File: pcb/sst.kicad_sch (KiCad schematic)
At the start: 0 parts

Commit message: кристалл и I2C на схеме
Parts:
- added C1, C2: C, symbol Device_GOST:C
- added R? (x2): R, symbol Device_GOST:R
- added U1: ATmega328P-P, Package_DIP:DIP-28_W7.62mm, symbol sst:ATmega328P-P
- added X?: CONN_I2C, symbol sst:CONN_I2C
- added ZQ1: ZQ_CRYSTAL, symbol Device_GOST:ZQ_CRYSTAL
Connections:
- new net: R?.1, U1.2 (PD0), X?.1, X?.2
- new net: R?.1, U1.3 (PD1), X?.3, X?.4
- new net: C1.1, C2.2, U1.10 (XTAL2/PB7), U1.22 (GND), U1.8 (GND), U1.9 (XTAL1/PB6), ZQ1.1, ZQ1.2
- new net +5V: R?.2, R?.2, X?.6, X?.7
- new net GND: C1.2, C2.1, X?.5, X?.8

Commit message: placed buzzer
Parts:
- added HA?: Buzzer, symbol sst:Buzzer
- added HL?: HL_LED, symbol Device_GOST:HL_LED
- added R? (x2): R, symbol Device_GOST:R
- added SA?: SA_SPDT, symbol Device_GOST:SA_SPDT
- added VT?: 2N7000, Package_TO_SOT_THT:TO-92, symbol sst:2N7000
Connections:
- net +5V: now also R?.2, SA?.2
- net GND: now also R?.1, VT?.1 (S1)
- net SDA: now reaches R?.1, U1.2 (PD0), X?.1, X?.2
- net SCL: now reaches R?.1, U1.3 (PD1), X?.3, X?.4
- net at U1.4 (PD2): now also R?.2, VT?.2 (G1)
- new net: HA?.1 (+), SA?.1
- new net: HA?.2 (-), HL?.1 (K), VT?.6 (D1)
- new net: HL?.2 (A), R?.1

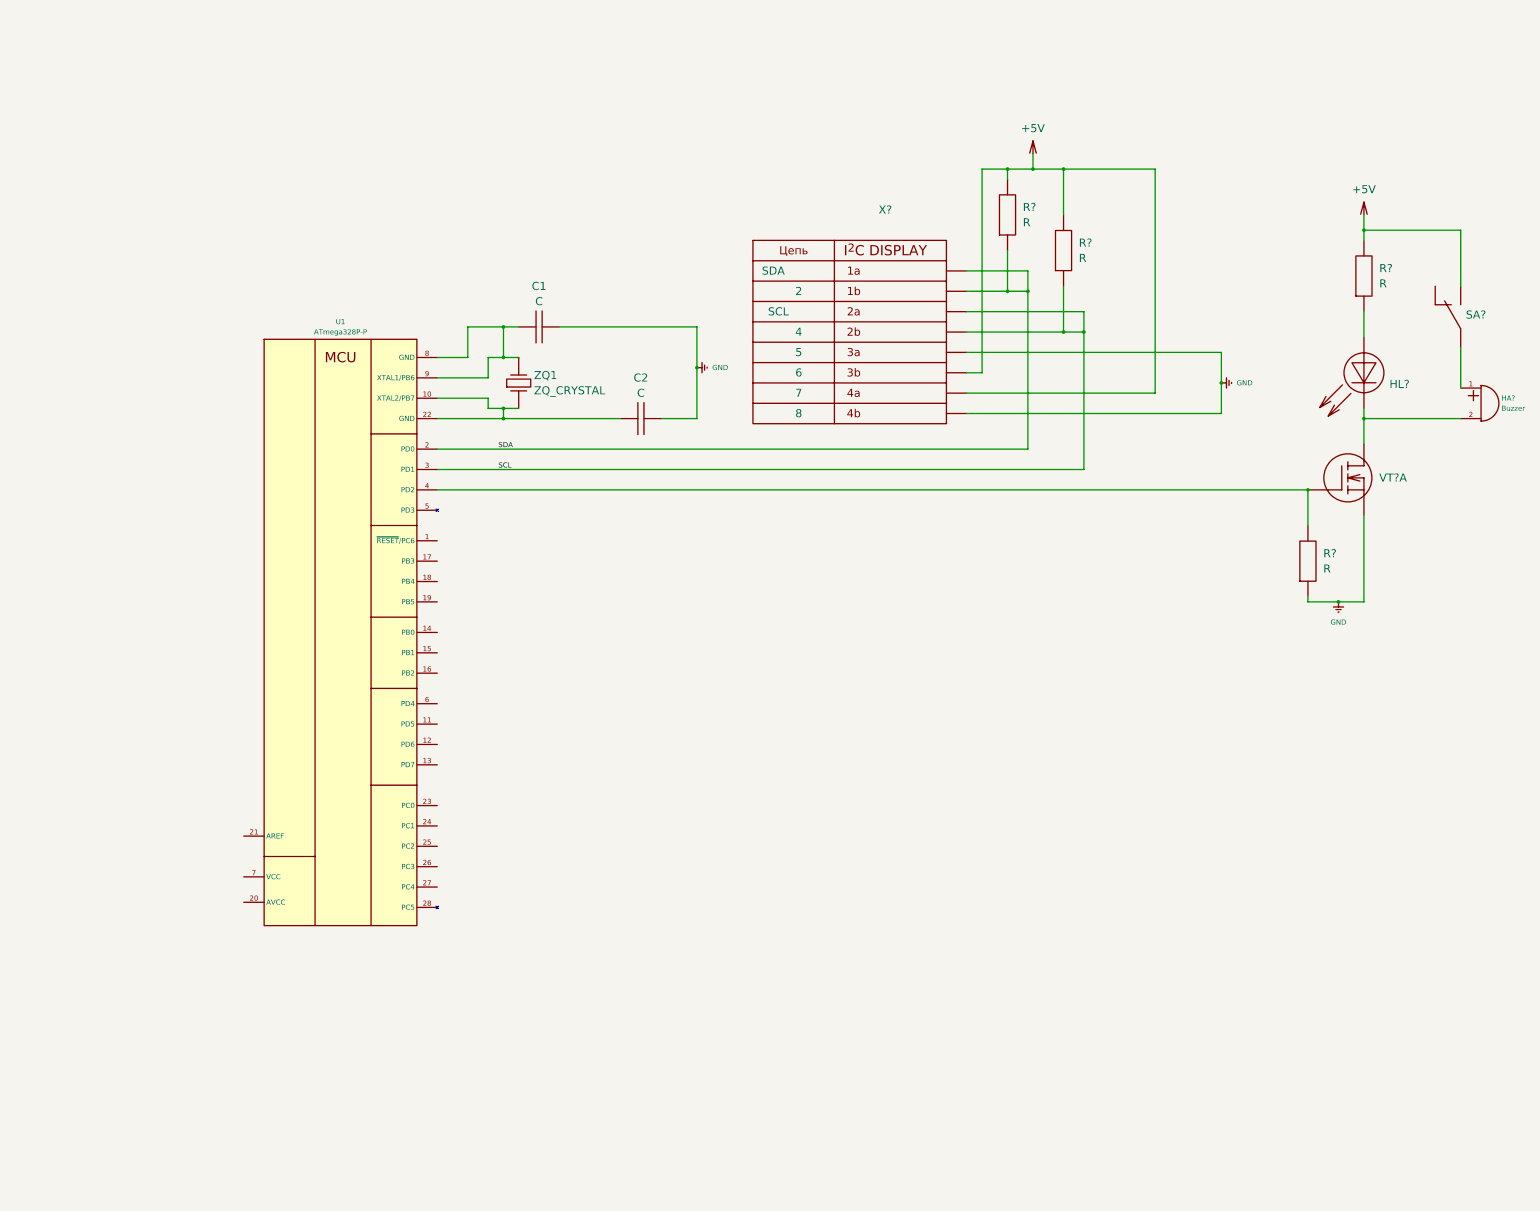
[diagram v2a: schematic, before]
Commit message: Входы на микроконтроллере
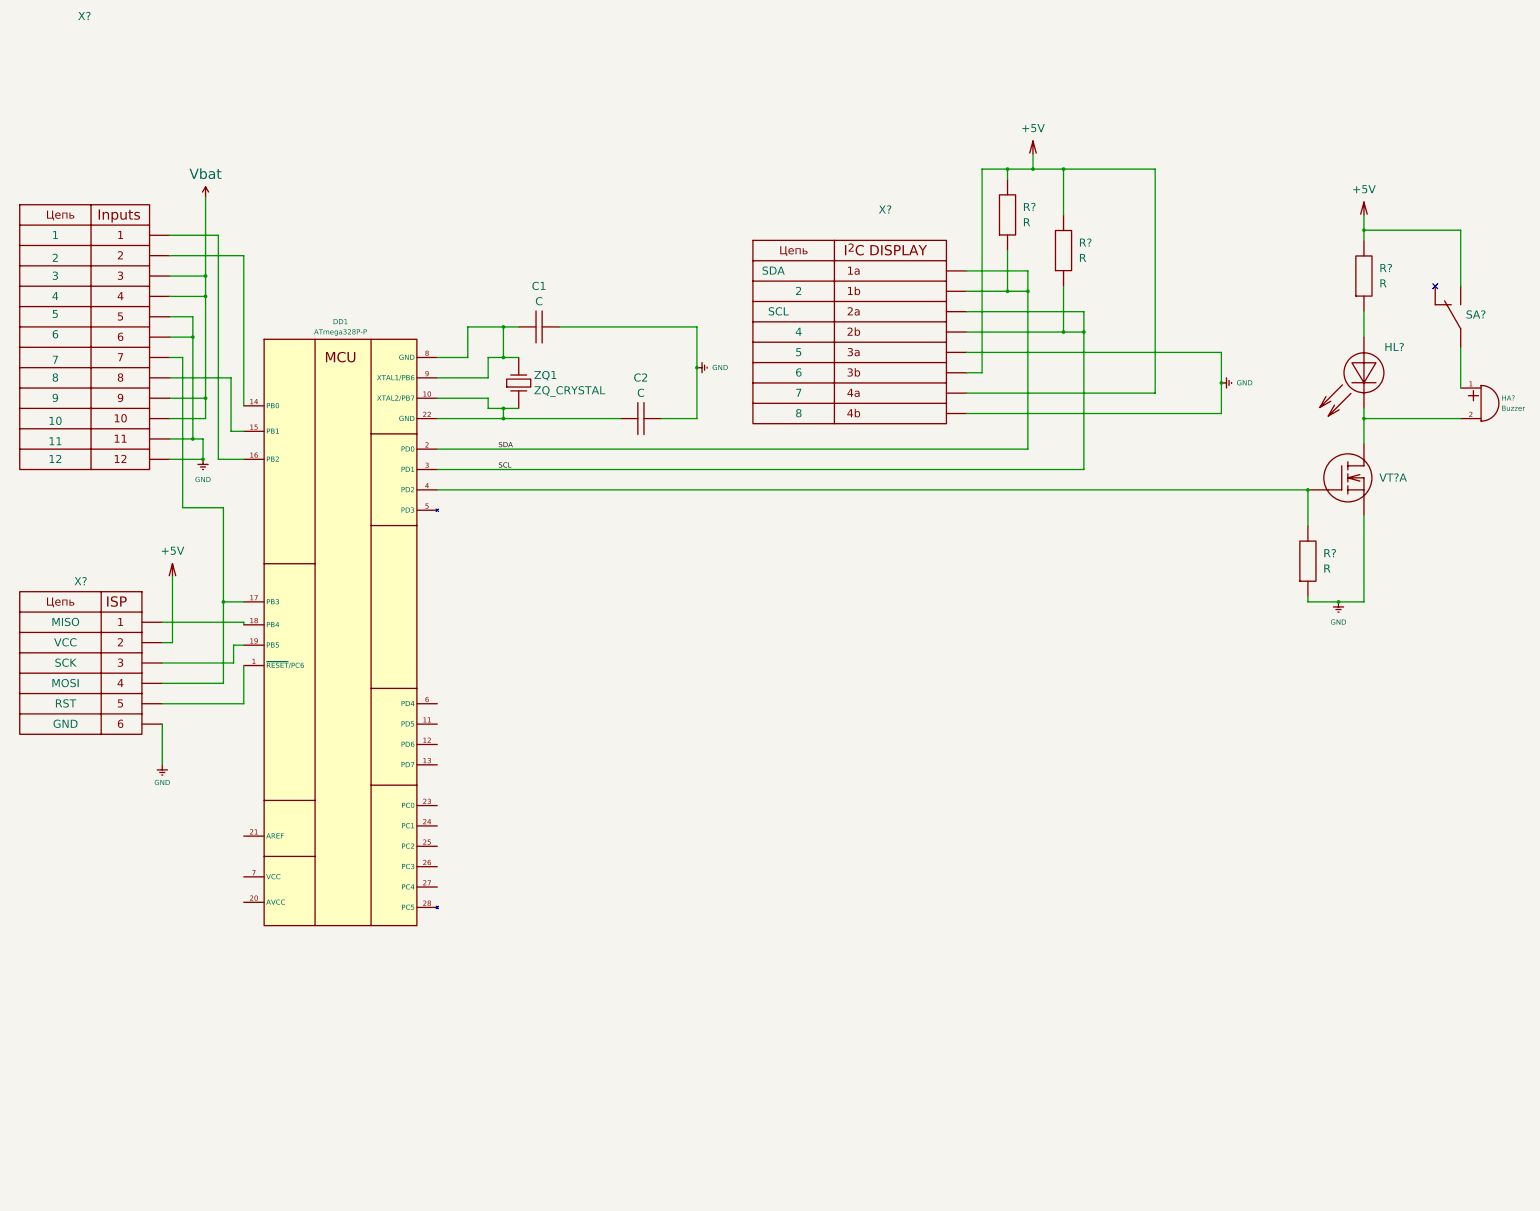
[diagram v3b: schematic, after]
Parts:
- added X?: CONN_SPI, symbol sst:CONN_SPI
- added X?: CONN_INPUTS, symbol sst:CONN_INPUTS
- renumbered U1 to DD1
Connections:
- net +5V: now also X?.2
- net GND: now also X?.11, X?.12, X?.5, X?.6, X?.6
- net at DD1.1 (~{RESET}/PC6): now also X?.5
- net at DD1.14 (PB0): now also X?.2
- net at DD1.15 (PB1): now also X?.8
- net at DD1.16 (PB2): now also X?.1
- net at DD1.17 (PB3): now also X?.4, X?.7
- net at DD1.18 (PB4): now also X?.1
- net at DD1.19 (PB5): now also X?.3
- new net Vbat: X?.10, X?.3, X?.4, X?.9
- no-connect marks 0 -> 1

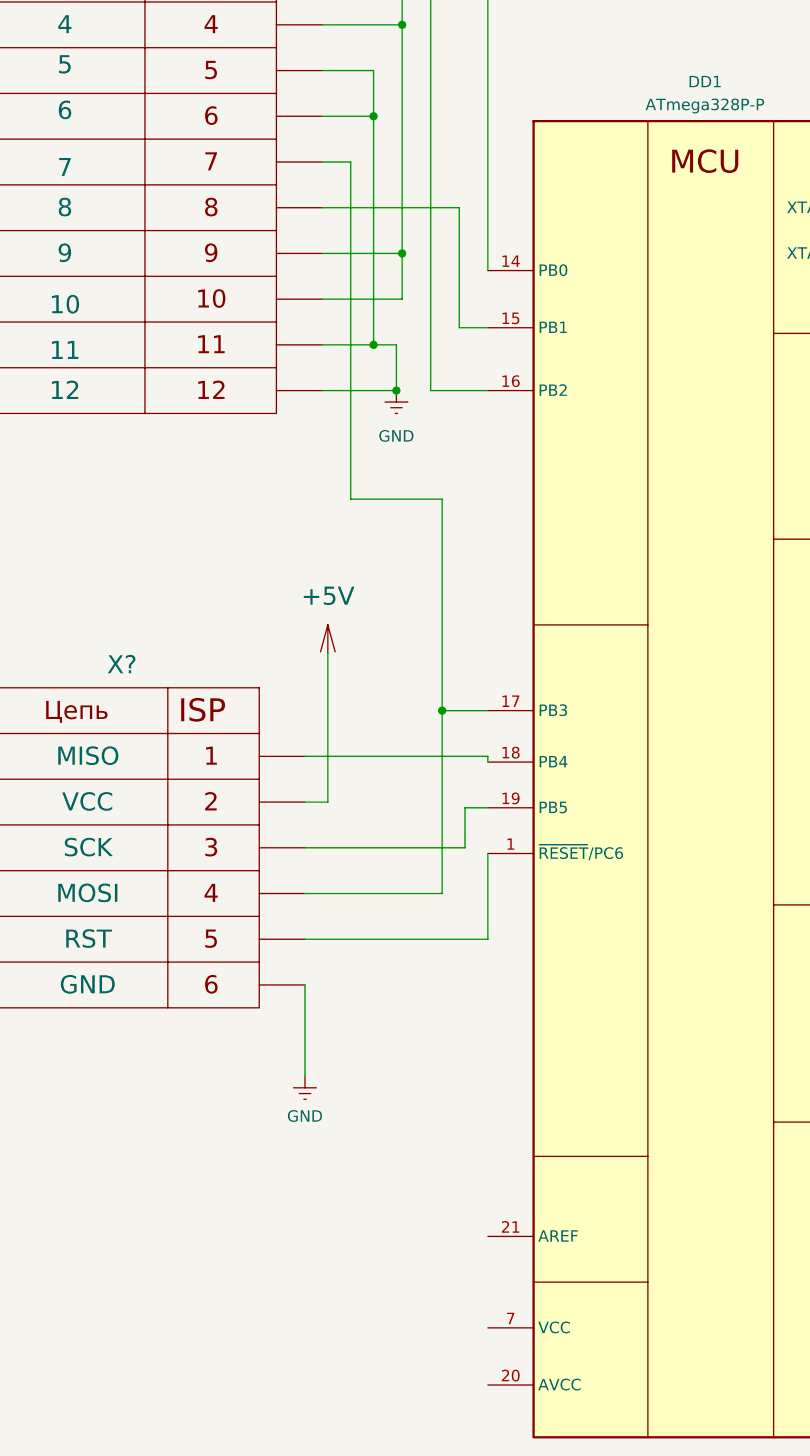
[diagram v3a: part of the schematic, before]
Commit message: все входы микроконтроллера готовы
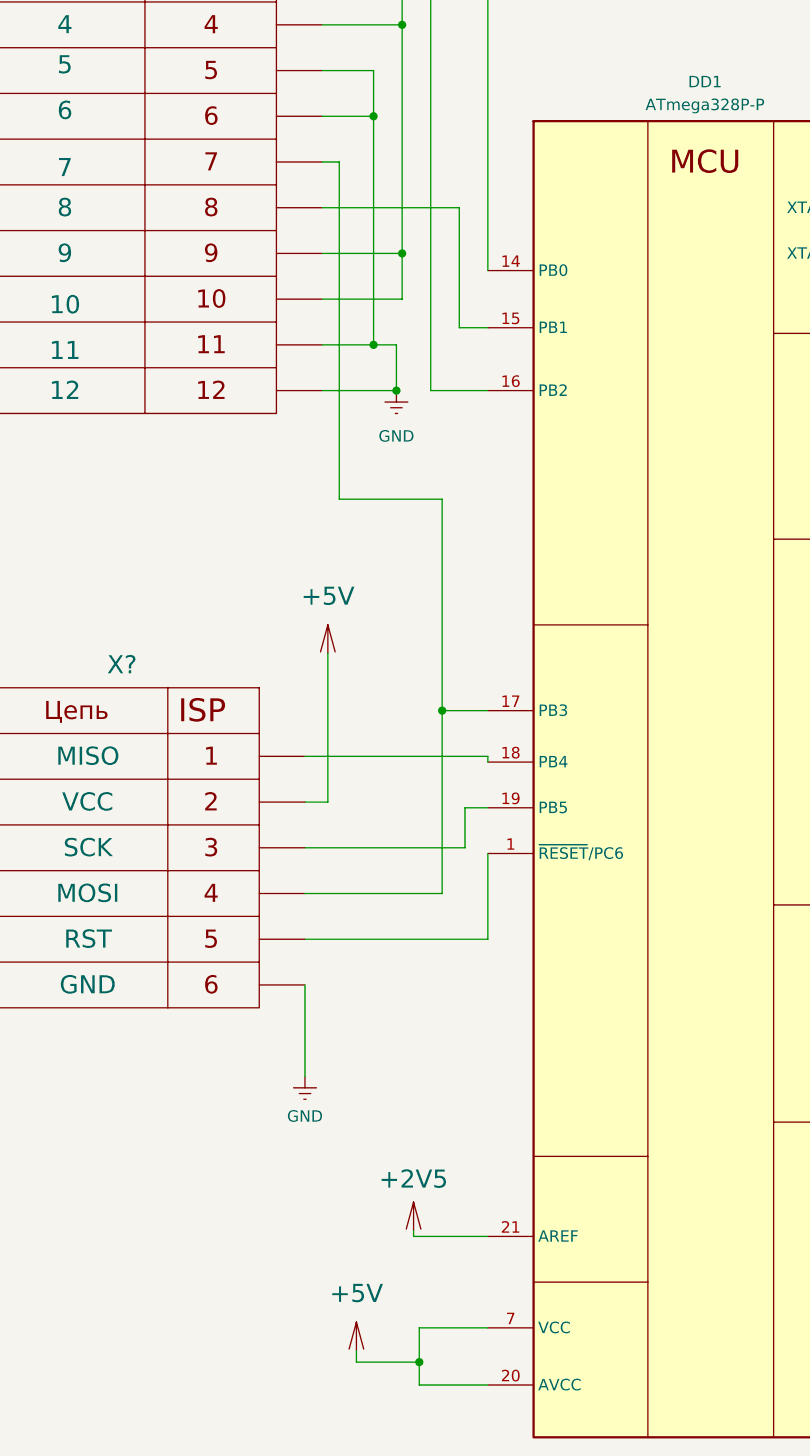
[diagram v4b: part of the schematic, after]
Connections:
- net +5V: now also DD1.20 (AVCC), DD1.7 (VCC)
- net +2V5: now reaches DD1.21 (AREF)
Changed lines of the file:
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@@
+	)
+	(junction
+		(at 76.2 201.93)
+		(diameter 0)
+		(color 0 0 0 0)
 	)
 	(junction
@@
 	(wire
 		(pts
-			(xy 65.405 68.58) (xy 68.58 68.58)
+			(xy 65.405 68.58) (xy 67.31 68.58)
 		)
 		(stroke
@@
 	(wire
 		(pts
+			(xy 69.215 201.93) (xy 76.2 201.93)
+		)
+		(stroke
+			(width 0)
+			(type default)
+		)
+	)
+	(wire
+		(pts
 			(xy 148.59 81.28) (xy 148.59 83.82)
 		)
@@
 	(wire
 		(pts
+			(xy 75.565 187.325) (xy 75.565 187.96)
+		)
+		(stroke
+			(width 0)
+			(type default)
+		)
+	)
+	(wire
+		(pts
 			(xy 327.66 67.31) (xy 327.66 74.93)
 		)
@@
 	(wire
 		(pts
+			(xy 75.565 187.96) (xy 83.82 187.96)
+		)
+		(stroke
+			(width 0)
+			(type default)
+		)
+	)
+	(wire
+		(pts
 			(xy 77.47 38.1) (xy 77.47 93.98)
 		)
@@
 	(wire
 		(pts
+			(xy 76.2 201.93) (xy 76.2 204.47)
+		)
+		(stroke
+			(width 0)
+			(type default)
+		)
+	)
+	(wire
+		(pts
 			(xy 274.32 21.59) (xy 280.67 21.59)
 		)
@@
 	(wire
 		(pts
+			(xy 83.82 198.12) (xy 76.2 198.12)
+		)
+		(stroke
+			(width 0)
+			(type default)
+		)
+	)
+	(wire
+		(pts
 			(xy 81.28 144.78) (xy 81.28 140.335)
 		)
@@
 	(wire
 		(pts
-			(xy 68.58 68.58) (xy 68.58 106.045)
+			(xy 67.31 68.58) (xy 67.31 106.045)
 		)
 		(stroke
@@
 	(wire
 		(pts
+			(xy 76.2 198.12) (xy 76.2 201.93)
+		)
+		(stroke
+			(width 0)
+			(type default)
+		)
+	)
+	(wire
+		(pts
 			(xy 63.5 149.86) (xy 78.74 149.86)
 		)
@@
 	(wire
 		(pts
+			(xy 69.215 200.66) (xy 69.215 201.93)
+		)
+		(stroke
+			(width 0)
+			(type default)
+		)
+	)
+	(wire
+		(pts
 			(xy 349.25 129.54) (xy 356.87 129.54)
 		)
@@
 	(wire
 		(pts
+			(xy 76.2 204.47) (xy 83.82 204.47)
+		)
+		(stroke
+			(width 0)
+			(type default)
+		)
+	)
+	(wire
+		(pts
 			(xy 139.7 60.96) (xy 148.59 60.96)
 		)
@@
 	(wire
 		(pts
-			(xy 68.58 106.045) (xy 78.74 106.045)
+			(xy 67.31 106.045) (xy 78.74 106.045)
 		)
 		(stroke
@@
 	(symbol
 		(lib_id "power_GOST:+5V")
+		(at 69.215 200.66 0)
+		(unit 1)
+		(exclude_from_sim no)
+		(in_bom yes)
+		(on_board yes)
+		(dnp no)
+		(fields_autoplaced yes)
+		(property "Reference" "#PWR010"
+			(at 69.215 203.2 0)
+			(effects
+				(font
+					(size 2.0066 2.0066)
+				)
+				(hide yes)
+			)
+		)
+		(property "Value" "+5V"
+			(at 69.215 194.31 0)
+			(effects
+				(font
+					(size 2.0066 2.0066)
+				)
+			)
+		)
+		(property "Footprint" ""
+			(at 69.215 197.485 90)
+			(effects
+				(font
+					(size 2.4892 2.4892)
+				)
+			)
+		)
+		(property "Datasheet" ""
+			(at 69.215 197.485 0)
+			(effects
+				(font
+					(size 2.4892 2.4892)
+				)
+				(hide yes)
+			)
+		)
+		(property "Description" ""
+			(at 69.215 200.66 0)
+			(effects
+				(font
+					(size 1.27 1.27)
+				)
+				(hide yes)
+			)
+		)
+		(pin "1"
+		)
+		(instances
+			(project ""
+				(path "/d486a0a8-b0b2-426a-9635-bf463f56fa2d"
+					(reference "#PWR010")
+					(unit 1)
+				)
+			)
+		)
+	)
+	(symbol
+		(lib_id "power_GOST:+5V")
 		(at 363.22 33.02 0)
 		(unit 1)
@@
 					(unit 1)
 				)
+			)
+		)
+	)
+	(symbol
+		(lib_id "sst:+2V5")
+		(at 75.565 187.325 0)
+		(unit 1)
+		(exclude_from_sim no)
+		(in_bom yes)
+		(on_board yes)
+		(dnp no)
+		(fields_autoplaced yes)
+		(property "Reference" "#PWR011"
+			(at 75.565 189.865 0)
+			(effects
+				(font
+					(size 2.0066 2.0066)
+				)
+				(hide yes)
+			)
+		)
+		(property "Value" "+2V5"
+			(at 75.565 181.61 0)
+			(effects
+				(font
+					(size 2.0066 2.0066)
+				)
+			)
+		)
+		(property "Footprint" ""
+			(at 75.565 184.15 90)
+			(effects
+				(font
+					(size 2.4892 2.4892)
+				)
+			)
+		)
+		(property "Datasheet" ""
+			(at 75.565 184.15 0)
+			(effects
+				(font
+					(size 2.4892 2.4892)
+				)
+				(hide yes)
+			)
+		)
+		(property "Description" ""
+			(at 75.565 187.325 0)
+			(effects
+				(font
+					(size 1.27 1.27)
+				)
+				(hide yes)
+			)
+		)
+		(pin "1"
+		)
+		(instances
+			(project ""
+				(path "/d486a0a8-b0b2-426a-9635-bf463f56fa2d"
+					(reference "#PWR011")
+					(unit 1)
+				)

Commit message: опроцентовка
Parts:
- added R? (x3): R, symbol Device_GOST:R
- added R? (x4): R_POT1, symbol Device_GOST:R_POT1
- added SA?: ~, symbol sst:SA_SLIDE_DPDT
- added X?: CONN_INPUTS, symbol sst:CONN_OUTPUTS
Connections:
- net +2V5: now also R?.3, R?.3, R?.3, R?.3
- net GND: now also R?.1, R?.1, R?.1, R?.1, R?.2, SA?.1, X?.11, X?.12, X?.5, X?.6
- net Vbat: now also R?.1, SA?.5, X?.10, X?.3, X?.4, X?.9
- net at DD1.11 (PD5): now also X?.7
- net at DD1.12 (PD6): now also X?.1
- net at DD1.13 (PD7): now also X?.8
- net at DD1.18 (PB4), X?.1: now also X?.2
- net at DD1.23 (PC0): now also R?.2
- net at DD1.24 (PC1): now also R?.2
- net at DD1.25 (PC2): now also R?.2
- net at DD1.26 (PC3): now also R?.2
- net at DD1.27 (PC4): now also R?.1, R?.2
- net at DD1.6 (PD4): now also SA?.3
- new net: R?.1, R?.2
- no-connect marks 1 -> 3
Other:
- title: Система тестирования\n сервоприводов квадрокоптера ->  «Система тестирования\n сервоприводов квадрокоптера» \n cхема электрическая принципиальная

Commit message: основная надпись (пока без литеры)
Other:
- title:  «Система тестирования\n сервоприводов квадрокоптера» \n cхема электрическая принципиальная ->  «Система тестирования\n сервоприводов квадрокоптера» 
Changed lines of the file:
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@@
 	(paper "A3")
 	(title_block
-		(title " «Система тестирования\\n сервоприводов квадрокоптера» \\n cхема электрическая принципиальная")
+		(title " «Система тестирования\\n сервоприводов квадрокоптера» ")
 		(date "2024-10-02")
-		(comment 1 "ГУИР 467993.013 Э3")
+		(comment 1 "467993.013 Э3")
 		(comment 2 "Корякин")
 	)
